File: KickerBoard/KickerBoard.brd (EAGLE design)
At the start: 75 x 50 mm, 126 parts, among them IC1 MAX3051ESA+, IC2 TPD4S014DSQR, J1 SM03B-ZESS-TB, J2 J_USB_MICROAB_HIROSE_ZX62-AB-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, Q1 TK12P60W, Q4 BSS138, Q5 BSP130, Q6 ZXTN08400BFF, U1 LPC1549JBD48, U10 AD8601, U11 ADCMP350YKSZ, U12 MIC5219-3.3YMM, U2 LM5160QPWPRQ1, U3 UCC27212DPRT, U4 UCC27512DRSR, U5 IC-AD_ADR5041, U7 LT6108-2, U8 UCC27524DGN-NOPAD, U9 INA213, Y1 FA238V

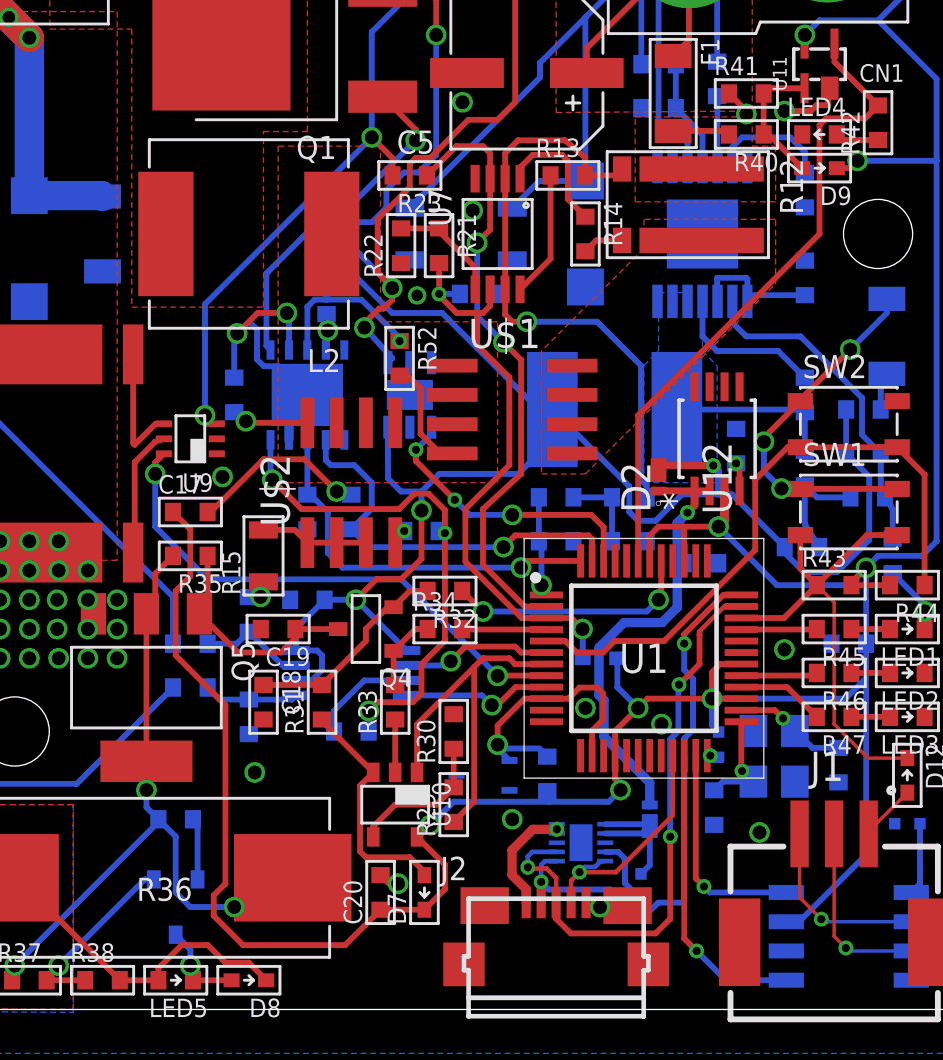
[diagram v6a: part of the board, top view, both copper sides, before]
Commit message: [fix]キッカーボードを25[V]仕様に変更(部品表はまだ)
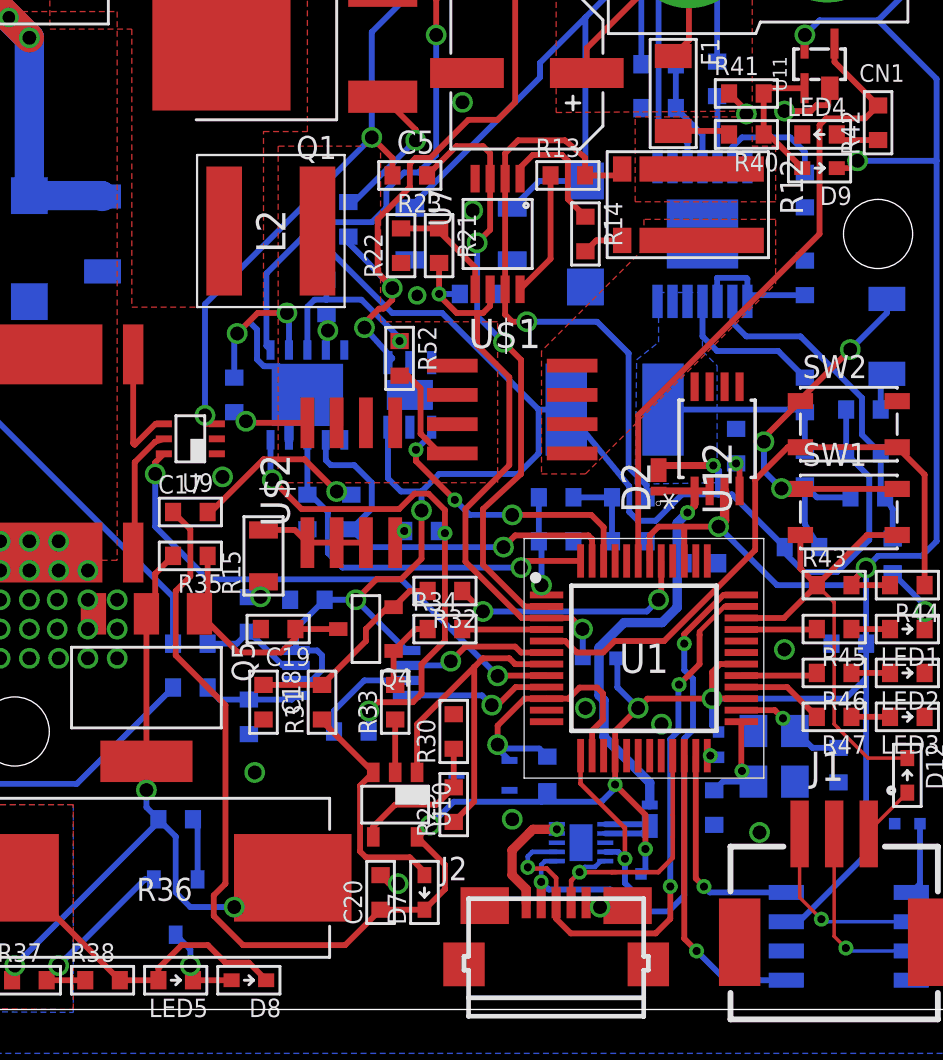
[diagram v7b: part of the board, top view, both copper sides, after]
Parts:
- C1: value 0.33n -> 0.47n
- C6: value 0.22u -> 4.7u
- D1: value SMAJ54A -> SMAJP4KE30A
- L1: value 47u -> 15u; device Passive:L6060 -> Passive:L4949
- L2: value 5.6u -> 8.2u; device Passive:L8682 -> SRP6060FA-220M:SRP6060FA220M
- R10: value 100k -> 33k
- R11: value 4.7k -> 3.3k
- R21: value 2.4k -> 3.3k
- R22: value 560 -> 750
- R3: value 13k -> 10k
- moved L2 0.96 mm to (44.8, 33.8), turned to 270 degrees
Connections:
- removed net N$51: IC2.4, R49.1
- new net USBACK: IC2.4, R49.1, U1.13
- net +3V3: now also R49.2
- net +5V: no longer R49.2
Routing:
- net USBACK: track 0.00 -> 8.30 mm, vias 0 -> 1
- net +3V3: track 191.4 -> 195.6 mm, vias 10 -> 11
- net N$51: track 3.02 -> 0.00 mm
- net +5V: track 6.27 -> 4.03 mm
- net ID: track 10.4 -> 11.7 mm
- net N$8: track 7.28 -> 7.88 mm

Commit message: [fix]ファイルが壊れてた
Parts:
- removed R15: 10, Passive:2012
- C1, C11, C12, C13, C14, C16, C17, C18, C19, C2, C20, C22, C3, C4, C7: device Passive:1608 -> MotorDriver:C1005
- C10, C9: device Passive:2012 -> MotorDriver:C1005
- C15: value (none) -> 0.1u; device Passive:1608 -> MotorDriver:C1005
- C21: device Passive:3216 -> MotorDriver:C3216
- C23, C24: value (none) -> 10p; device MotorDriver:C1608 -> MotorDriver:C1005
- C6: device Passive:1608 -> MotorDriver:C1608
- C8: device Passive:3216 -> MotorDriver:C1608
- D1, D4: device Diode:DO-214AC -> MotorDriver:DO-214AC
- D10, D7, D8, D9: device Diode:SOD523 -> MotorDriver:DIODE_SOD523
- D12: device MotorDriver:MOTORDRIVER_DIODE_SOD523 -> MotorDriver:DIODE_SOD523
- LED4, LED5: device Opto:1608 -> MotorDriver:LED1608
- R1, R10, R11, R16, R17, R18, R2, R20, R21, R22, R23, R26, R27, R29, R3, R30, R31, R32, R33, R35, R37, R38, R39, R40, R41, R5, R50, R6, R8, R9: device Passive:1608 -> MotorDriver:R1005
- R13, R14, R34, R4, R7: device Passive:1608 -> MotorDriver:R1608
- R42: value 220 -> 330; device Passive:1608 -> MotorDriver:R1005
- R43, R44: device MotorDriver:R1608 -> MotorDriver:R1005
- R45, R46, R47: value 100 -> 330; device MotorDriver:R1608 -> MotorDriver:R1005
- U1: device MotorDriver_Rev1:LPC1549JBD48_QFP50P900X900X160-48N -> MotorDriver:QFP48
- moved C11 3.49 mm to (60.5, 17.5), turned to 90 degrees
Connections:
- removed net N$23: R15.2, U$2.1, U$2.2, U$2.3
- net GND: now also U$2.1, U$2.2, U$2.3; no longer R15.1
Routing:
- net +3V3: track 195.6 -> 224.8 mm, vias 11 -> 12
- net GND: track 57.4 -> 43.9 mm, vias 45 -> 46
- net +12V: track 93.5 -> 102.6 mm, vias 4 -> 6
- net N$23: track 4.67 -> 0.00 mm
- net CURRENT_POS: track 5.58 -> 4.20 mm
- net N$1: track 1.66 -> 2.54 mm
- net V+: track 62.7 -> 61.9 mm
- net CURRENT_NEG: track 5.60 -> 6.15 mm
- net N$41: track 8.20 -> 8.72 mm
